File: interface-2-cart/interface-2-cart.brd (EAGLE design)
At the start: 38.7 x 40.1 mm, 44 parts, among them U3 W25Q128JVSIQ, U4 SN74LVC245ADBR, U5 SN74LVC245ADBR, U6 SN74LVCC4245APWR, X2 TSX-32250, X3 DNP

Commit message: New version of IF2 cart, fixed bug
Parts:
- removed C10: 100nF, res-small-footprint:C0402
- removed C12: 1uF, res-small-footprint:C0402
- removed U6: SN74LVCC4245APWR, SN74LVCC4245APWR:SOP65P640X120-24N
- added C6: 4u7, res-small-footprint:C0402
- added R1, R2, R3, R4, R5, R6, R7, R8: 10K, res-small-footprint:0402
- added U1: SN74LVC245ADBR, SN74LVC245ADBR:SOP65P780X200-20N
- C1: value 100nF -> 4u7
- C23: value 2u2 -> 4u7
- C24: value 2u2 -> 100nF
- C28: value 10uF -> 4u7
- moved C2 9.41 mm to (10.5, 15.7)
- moved C18 4.33 mm to (1.91, 27.4), turned to 90 degrees
- moved C28 4.15 mm to (13.7, 34.8)
- moved D2 4.05 mm to (27.9, 24.1)
- moved D3 3.43 mm to (30.7, 24.1)
- moved R24 2.81 mm to (26.5, 35.8), turned to 0 degrees
- moved U3 1.40 mm to (7.18, 28.7)
- moved C19 1.26 mm to (14.2, 29.0), turned to 180 degrees
- moved C21 1.20 mm to (13.5, 32.6)
- moved C27 0.81 mm to (17.9, 27.6), turned to 225 degrees
- moved L1 0.51 mm to (12.1, 34.8), turned to 90 degrees
- moved C16 0.38 mm to (20.6, 27.4)
- moved C22 0.25 mm to (23.1, 38.0)
- moved C13 0.13 mm to (27.9, 28.6)
- moved C14 0.13 mm to (27.9, 34.2)
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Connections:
- net /ROMCS_3V3: now also U1.1; no longer U6.2
- net 3V3: now also C6.P$1; no longer C10.P$1, C12.P$2, U6.24
- net D0: now also R8.P$2, U1.9; no longer U6.21
- net D0_5V: now also U1.11; no longer U6.3
- net D1: now also R7.P$2, U1.8; no longer U6.20
- net D1_5V: now also U1.12; no longer U6.4
- net D2: now also R6.P$2, U1.7; no longer U6.19
- net D2_5V: now also U1.13; no longer U6.5
- net D3: now also R5.P$2, U1.6; no longer U6.18
- net D3_5V: now also U1.14; no longer U6.6
- net D4: now also R4.P$2, U1.5; no longer U6.17
- net D4_5V: now also U1.15; no longer U6.7
- net D5: now also R3.P$2, U1.4; no longer U6.16
- net D5_5V: now also U1.16; no longer U6.8
- net D6: now also R2.P$2, U1.3; no longer U6.15
- net D6_5V: now also U1.17; no longer U6.9
- net D7: now also R1.P$2, U1.2; no longer U6.14
- net D7_5V: now also U1.18; no longer U6.10
- net GND: now also C6.P$2, R1.P$1, R2.P$1, R3.P$1, R4.P$1, R5.P$1, R6.P$1, R7.P$1, R8.P$1, U1.10; no longer C10.P$2, C12.P$1, U6.11, U6.12, U6.13
- net ROMRQ_3V3: now also U1.19; no longer U6.22
- net VCC: now also U1.20; no longer U6.1
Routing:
- net D7: track 23.5 -> 46.8 mm
- net D6: track 25.1 -> 46.8 mm
- net D5: track 28.8 -> 47.1 mm
- net D0: track 28.7 -> 47.0 mm
- net D1: track 29.3 -> 46.8 mm
- net D2: track 29.6 -> 46.8 mm
- net 1V2: track 31.0 -> 14.1 mm
- net D4: track 32.2 -> 47.3 mm
- net A11_5V: track 10.8 -> 25.3 mm, vias 0 -> 2
- net A0_5V: track 11.0 -> 25.1 mm
- net D3: track 33.5 -> 47.3 mm
- net A1_5V: track 11.7 -> 25.0 mm
- net A2_5V: track 13.1 -> 25.0 mm
- net A9_5V: track 13.8 -> 25.3 mm
- net A10_5V: track 14.9 -> 25.3 mm
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- added copper zone on layer 15, net 1V2
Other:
- board text added: "ZXelerator V1.1 2025 Smashcat"
- board text removed: "ZXelerator V1.0 2025 Smashcat"

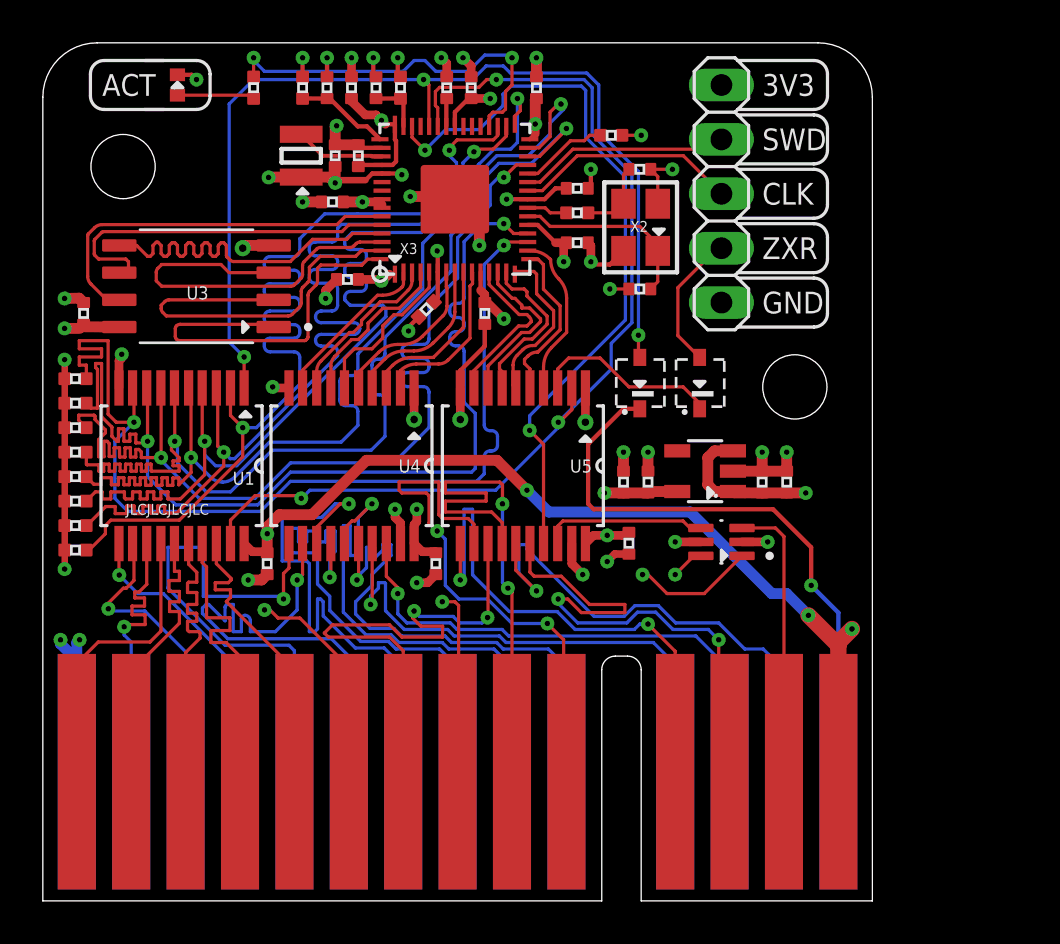
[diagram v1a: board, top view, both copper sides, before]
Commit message: Finished redesign of IF2 PCB - all data and address tracks now length matched, although whether that makes any difference... Submitted for production
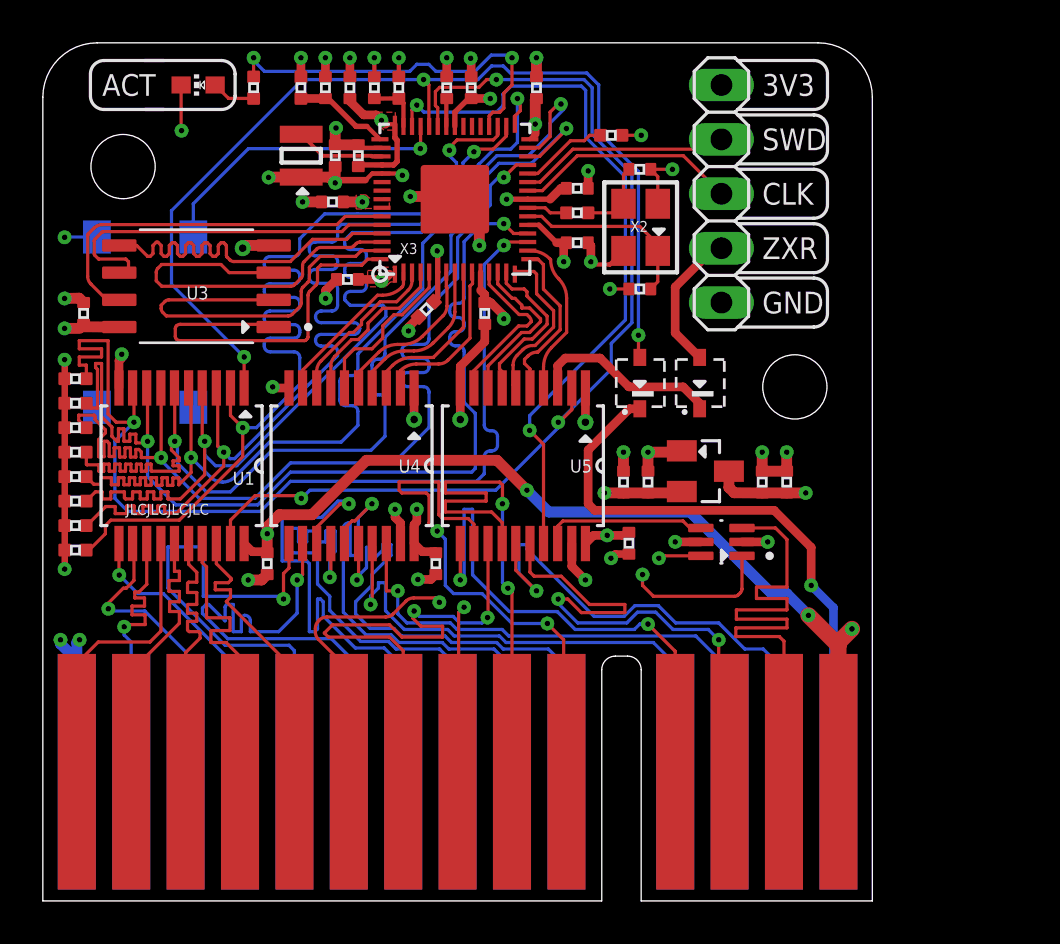
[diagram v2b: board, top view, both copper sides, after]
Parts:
- removed S_LED10: 20mA, led-0402:LED_VLMW15_VIS
- added ACT_LED: 20mA, 52101-101-REV-A_v16:LED_CHIP-LED0603MP
- added USER_BUTTON: PTS645SM43SMTR92LFS, PTS645SM43SMTR92LFS:PTS645(SMT)
- 3V3_REG2: value 3V3 -> MCP1703CB; device IC-packages_BIG-pack V1.0:NCP718BSN330T1G -> linear:SOT23
- moved C20 0.08 mm to (14.3, 38.0)
- moved C23 0.08 mm to (13.2, 38.0)
- moved C24 0.08 mm to (15.5, 38.0)
- moved R25 0.08 mm to (16.6, 38.0)
- moved R9 0.08 mm to (12.1, 38.0)
- turned 3V3_REG2 to 270 degrees
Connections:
- new net USER_BUT: USER_BUTTON.3, X3.42
- net 3V3: now also 3V3_REG2.2; no longer 3V3_REG2.5
- net GND: now also 3V3_REG2.1, ACT_LED.C, USER_BUTTON.1; no longer 3V3_REG2.2, S_LED10.C
- net N$6: now also ACT_LED.A; no longer S_LED10.A
- net VCC: no longer 3V3_REG2.1
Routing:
- net USER_BUT: track 0.00 -> 14.3 mm, vias 0 -> 1
- net A15_5V: track 13.1 -> 25.2 mm
- net A14_5V: track 33.1 -> 27.3 mm
- net VCC: track 48.2 -> 45.4 mm
- net GND: track 74.0 -> 76.2 mm, vias 38 -> 39
- net N$6: track 3.62 -> 2.06 mm
- net 3V3: track 36.1 -> 35.1 mm
- net /ROMCS_3V3: track 47.8 -> 48.7 mm
- added copper zone on layer 1, net 3V3

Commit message: Final(?) design of IF2 PCB.
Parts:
- removed U4, U5: SN74LVC245ADBR, SN74LVC245ADBR:SOP65P780X200-20N
- added U0, U2: SOP65P640X110-20N, SOP65P640X110-20N:SOP65P640X110-20N
- D2, D3: value BZX384C5V6-E3-08 -> (none); device BZX384C5V6-E3-08:SOD-323 -> adafruit:SOD-323F
- U1: value SN74LVC245ADBR -> SOP65P640X110-20N; device SN74LVC245ADBR:SOP65P780X200-20N -> SOP65P640X110-20N:SOP65P640X110-20N
- moved U$2 13.5 mm to (18.3, 18.4), turned to 90 degrees
- moved U1 7.85 mm to (13.3, 16.4)
- moved R2 7.71 mm to (9.14, 16.4), turned to 90 degrees
- moved R1 7.44 mm to (7.49, 20.8)
- moved R4 6.38 mm to (0.89, 13.5), turned to 90 degrees
- moved R7 4.87 mm to (0.89, 18.4), turned to 270 degrees
- moved R5 4.74 mm to (0.89, 16.3), turned to 90 degrees
- moved R3 4.49 mm to (5.46, 20.8)
- moved ACT_LED 4.32 mm to (7.25, 33.8)
- moved C1 4.32 mm to (25.0, 29.0)
- moved C15 4.32 mm to (25.0, 26.4)
- moved C19 4.32 mm to (14.2, 24.7)
- moved C21 4.32 mm to (13.5, 28.3)
- moved C28 4.32 mm to (13.7, 30.5)
- moved C6 4.32 mm to (14.7, 30.5)
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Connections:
- net /RESET_3V3: now also U2.B1; no longer U5.17
- net /ROMCS_3V3: now also U0.DIR; no longer U1.1
- net 3V3: now also U1.VCC, U2.VCC; no longer U4.20, U5.20
- net A0: now also U1.A7; no longer U4.9
- net A0_5V: now also U1.B7; no longer U4.11
- net A1: now also U1.A6; no longer U4.8
- net A10: now also U2.A5; no longer U5.7
- net A10_5V: now also U2.B5; no longer U5.13
- net A11: now also U2.A4; no longer U5.6
- net A11_5V: now also U2.B4; no longer U5.14
- net A12: now also U2.A3; no longer U5.5
- net A12_5V: now also U2.B3; no longer U5.15
- net A13: now also U2.A2; no longer U5.4
- net A13_5V: now also U2.B2; no longer U5.16
- net A1_5V: now also U1.B6; no longer U4.12
- net A2: now also U1.A5; no longer U4.7
- net A2_5V: now also U1.B5; no longer U4.13
- net A3: now also U1.A4; no longer U4.6
- net A3_5V: now also U1.B4; no longer U4.14
- net A4: now also U1.A3; no longer U4.5
- net A4_5V: now also U1.B3; no longer U4.15
- net A5: now also U1.A2; no longer U4.4
- net A5_5V: now also U1.B2; no longer U4.16
- net A6: now also U1.A1; no longer U4.3
- net A6_5V: now also U1.B1; no longer U4.17
- net A7: now also U1.A0; no longer U4.2
- net A7_5V: now also U1.B0; no longer U4.18
- net A8: now also U2.A7; no longer U5.9
- net A8_5V: now also U2.B7; no longer U5.11
- net A9: now also U2.A6; no longer U5.8
- net A9_5V: now also U2.B6; no longer U5.12
- net D0: now also U0.A7; no longer U1.9
- net D0_5V: now also U0.B7; no longer U1.11
- net D1: now also U0.A6; no longer U1.8
- net D1_5V: now also U0.B6; no longer U1.12
- net D2: now also U0.A5; no longer U1.7
- net D2_5V: now also U0.B5; no longer U1.13
- net D3: now also U0.A4; no longer U1.6
- net D3_5V: now also U0.B4; no longer U1.14
- net D4: now also U0.A3; no longer U1.5
- net D4_5V: now also U0.B3; no longer U1.15
- net D5: now also U0.A2; no longer U1.4
- net D5_5V: now also U0.B2; no longer U1.16
- net D6: now also U0.A1; no longer U1.3
- net D6_5V: now also U0.B1; no longer U1.17
- net D7: now also U0.A0; no longer U1.2
- net D7_5V: now also U0.B0; no longer U1.18
- net GND: now also U0.GND, U1./OE, U1.DIR, U1.GND, U2./OE, U2.DIR, U2.GND; no longer U1.10, U4.1, U4.10, U4.19, U5.1, U5.10, U5.19
- net N$9: now also U2.A1; no longer U5.3
- net ROMRQ: now also U2.B0; no longer U5.18
- net ROMRQ_3V3: now also U0./OE, U2.A0; no longer U1.19, U5.2
- net VCC: now also U0.VCC; no longer U1.20
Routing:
- net VCC: track 45.4 -> 16.8 mm, vias 5 -> 6
- net A0_5V: track 25.2 -> 9.16 mm
- net A9_5V: track 25.3 -> 10.4 mm, vias 2 -> 0
- net A1_5V: track 25.1 -> 10.5 mm
- net D6: track 46.8 -> 33.9 mm
- net /MREQ: track 25.2 -> 13.1 mm
- net D5: track 47.1 -> 35.7 mm
- net A3_5V: track 25.3 -> 14.1 mm
- net D7: track 46.8 -> 35.7 mm
- net D2: track 46.8 -> 35.9 mm
- net A11_5V: track 25.3 -> 14.7 mm, vias 2 -> 0
- net A14_5V: track 27.3 -> 16.8 mm, vias 2 -> 0
- net D0: track 47.0 -> 36.5 mm
- net A10_5V: track 25.3 -> 15.6 mm
- net A4_5V: track 25.2 -> 15.6 mm
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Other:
- board size 38.7 x 40.1 mm -> 38.7 x 35.8 mm
- board text added: "ZXelerator V1.2 2025 Smashcat"
- board text removed: "ZXelerator V1.1 2025 Smashcat"
